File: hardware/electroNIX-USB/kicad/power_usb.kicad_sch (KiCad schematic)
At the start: 13 parts, among them J1 USB-C (USB 2.0), U1 USBLC6-2SC6, U2 AMS1117-3.3, U3 CH340C

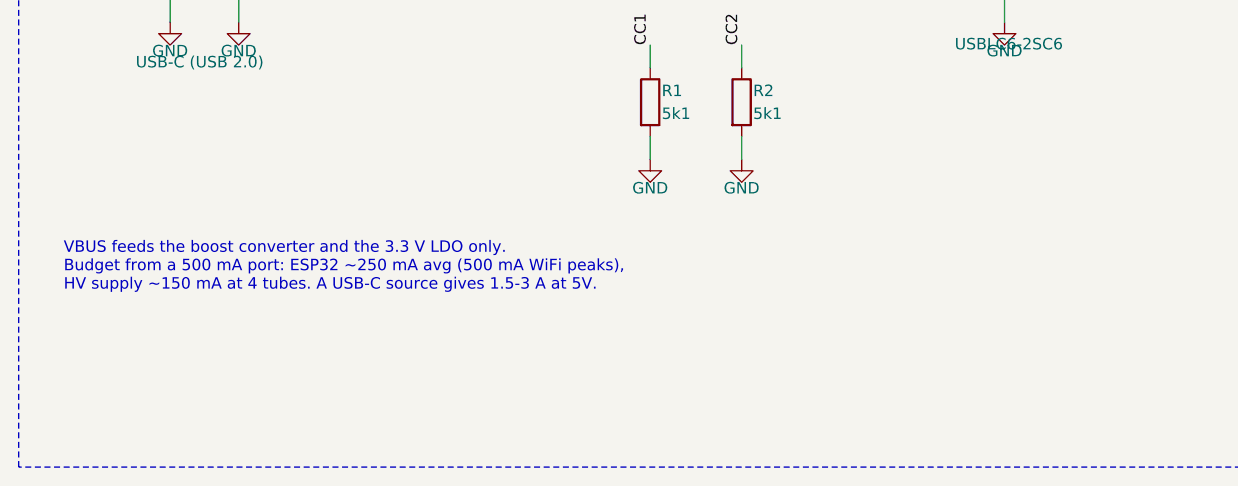
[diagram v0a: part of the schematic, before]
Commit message: electroNIX-USB: add 6-tube variant
The generator takes --tubes 4|6. The 6-tube build adds two anode switches
on IO12/IO15 and doubles the colon neons. It drops the buzzer and DS3231,
which matches the stock BOARD_ELECTRONIX_4_6T GPIO map, so no firmware
change is needed. HV supply, cathode drivers, ESP32, USB and power are
unchanged. Both projects are committed, with their own schematic PDF
and BOM.

Co-Authored-By: Claude Opus 5.5 <noreply@anthropic.com>
Claude-Session: https://claude.ai/code/session_01AFMfevKEKDGbci8uJGhf4W
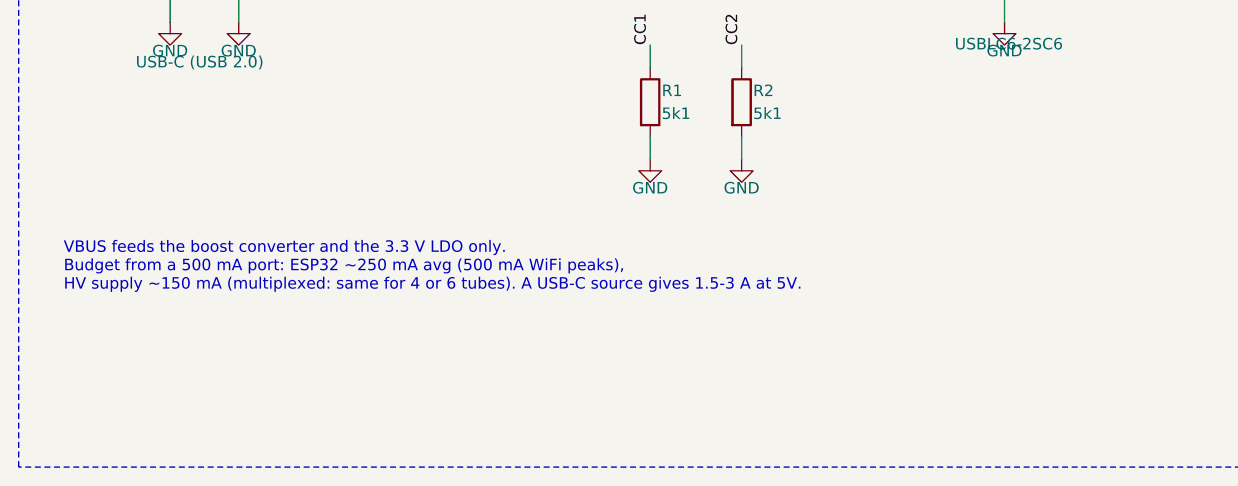
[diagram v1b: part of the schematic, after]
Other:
- note added: "VBUS feeds the boost converter and the 3.3 V LDO only. Budget from a 500 mA port: ESP32 ~250 mA avg (500 mA WiFi peaks), HV supply ~150 mA (multiplexed: same for 4 or 6 tubes). A USB-C source gives 1.5-3 A at 5V."
- note removed: "VBUS feeds the boost converter and the 3.3 V LDO only. Budget from a 500 mA port: ESP32 ~250 mA avg (500 mA WiFi peaks), HV supply ~150 mA at 4 tubes. A USB-C source gives 1.5-3 A at 5V."
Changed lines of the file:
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@@
       (justify left top))
 )
-  (text "VBUS feeds the boost converter and the 3.3 V LDO only.\nBudget from a 500 mA port: ESP32 ~250 mA avg (500 mA WiFi peaks),\nHV supply ~150 mA at 4 tubes. A USB-C source gives 1.5-3 A at 5V."
+  (text "VBUS feeds the boost converter and the 3.3 V LDO only.\nBudget from a 500 mA port: ESP32 ~250 mA avg (500 mA WiFi peaks),\nHV supply ~150 mA (multiplexed: same for 4 or 6 tubes). A USB-C source gives 1.5-3 A at 5V."
     (at 25 140 0)
     (effects
